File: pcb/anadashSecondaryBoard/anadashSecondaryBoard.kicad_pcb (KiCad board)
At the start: 2 copper layers, 198 x 35 mm, 12 parts, among them J2 LeftKeyConnector, J3 RightKeyConnector, J4 EncoderConnector, SW1 SW_Push, SW2 SW_Push, SW3 SW_Push, SW4 SW_Push, SW5 SW_Push, SW6 SW_Push, SW7 SW_Push, SW8 SW_Push, SW9 RotaryEncoder_Switch_MP

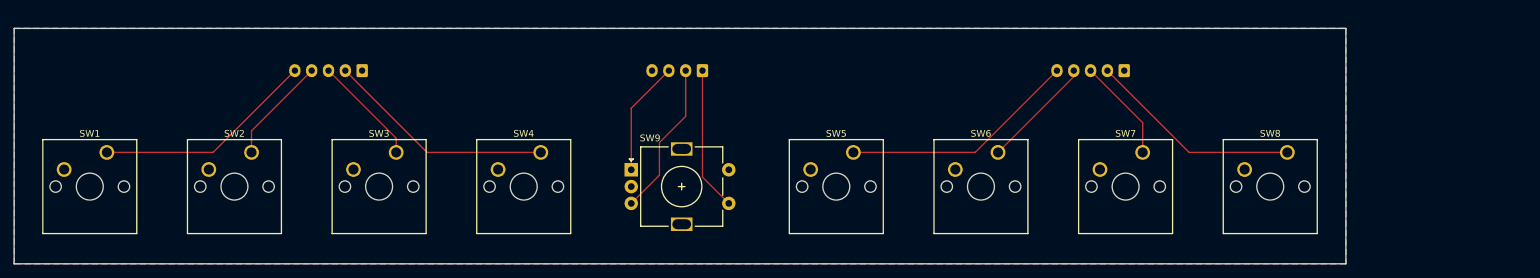
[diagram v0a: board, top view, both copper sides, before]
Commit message: Fixing alignment, improvements to pcb such as silkscreen.
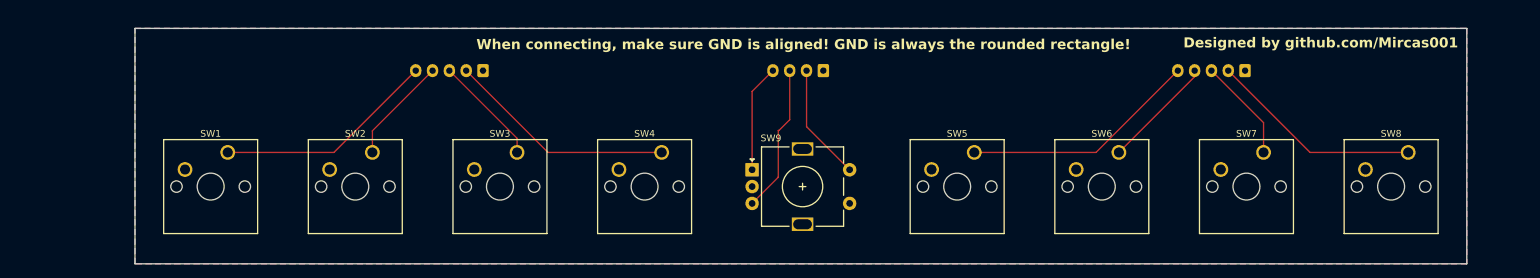
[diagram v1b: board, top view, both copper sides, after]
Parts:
- moved SW2 18.0 mm to (92.7, 90.6)
- moved SW4 18.0 mm to (135.7, 90.6)
- moved J2 18.0 mm to (109.2, 78.4)
- moved J3 18.0 mm to (222.5, 78.4)
- moved J4 18.0 mm to (159.8, 78.4)
- moved SW1 18.0 mm to (71.2, 90.6)
- moved SW3 18.0 mm to (114.2, 90.6)
- moved SW5 18.0 mm to (182.2, 90.6)
- moved SW6 18.0 mm to (203.7, 90.6)
- moved SW7 18.0 mm to (225.2, 90.6)
- moved SW8 18.0 mm to (246.7, 90.6)
- moved SW9 18.0 mm to (149.2, 93.1)
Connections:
- J4 pad 1: Net-(J4-Pin_1) -> GND
- J4 pad 4: GND -> Net-(J4-Pin_4)
- SW9 pad A: Net-(J4-Pin_3) -> Net-(J4-Pin_4)
- SW9 pad B: Net-(J4-Pin_2) -> Net-(J4-Pin_3)
- SW9 pad S1: Net-(J4-Pin_1) -> GND
- SW9 pad S2: GND -> Net-(J4-Pin_2)
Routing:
- net Net-(J4-Pin_1): track 21.4 -> 0.00 mm
- net Net-(J4-Pin_4): track 0.00 -> 16.0 mm
- net Net-(J4-Pin_2): track 23.1 -> 17.4 mm
- net Net-(J4-Pin_3): track 17.1 -> 22.1 mm
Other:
- board text added: "Designed by github.com/Mircas001"
- board text added: "When connecting, make sure GND is aligned! GND is always the rounded rectangle!"
- board text added: "When connecting, make sure GND is aligned! GND is always the rounded rectangle!r"

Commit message: both pcbs are done, but readme is bad
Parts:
- SW1, SW2, SW3, SW4, SW5, SW6, SW7, SW8: footprint Library:SW_Cherry_MX_1.00u_PCB -> footprints:SW_Cherry_MX_1.00u_PCB
- SW9: footprint Library:RotaryEncoder_Alps_EC11E-Switch_Vertical_H20mm -> footprints:RotaryEncoder_Alps_EC11E-Switch_Vertical_H20mm
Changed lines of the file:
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@@
 		)
 	)
-	(footprint "Library:SW_Cherry_MX_1.00u_PCB"
+	(footprint "footprints:SW_Cherry_MX_1.00u_PCB"
 		(layer "F.Cu")
 		(at 135.733572 90.56)
@@
 		)
 	)
-	(footprint "Library:RotaryEncoder_Alps_EC11E-Switch_Vertical_H20mm"
+	(footprint "footprints:RotaryEncoder_Alps_EC11E-Switch_Vertical_H20mm"
 		(layer "F.Cu")
 		(at 149.178572 93.14)
@@
 		(model "../3dmodels/EC11.STEP"
 			(offset
-				(xyz 7.25 -2.5 0)
+				(xyz 7.5 -2.5 0)
 			)
 			(scale
@@
 		)
 	)
-	(footprint "Library:SW_Cherry_MX_1.00u_PCB"
+	(footprint "footprints:SW_Cherry_MX_1.00u_PCB"
 		(layer "F.Cu")
 		(at 92.723572 90.56)
@@
 		)
 	)
-	(footprint "Library:SW_Cherry_MX_1.00u_PCB"
+	(footprint "footprints:SW_Cherry_MX_1.00u_PCB"
 		(layer "F.Cu")
 		(at 203.708572 90.56)
@@
 		)
 	)
-	(footprint "Library:SW_Cherry_MX_1.00u_PCB"
+	(footprint "footprints:SW_Cherry_MX_1.00u_PCB"
 		(layer "F.Cu")
 		(at 182.203572 90.56)
@@
 		)
 	)
-	(footprint "Library:SW_Cherry_MX_1.00u_PCB"
+	(footprint "footprints:SW_Cherry_MX_1.00u_PCB"
 		(layer "F.Cu")
 		(at 225.213572 90.56)
@@
 		)
 	)
-	(footprint "Library:SW_Cherry_MX_1.00u_PCB"
+	(footprint "footprints:SW_Cherry_MX_1.00u_PCB"
 		(layer "F.Cu")
 		(at 114.228572 90.56)
@@
 		)
 	)
-	(footprint "Library:SW_Cherry_MX_1.00u_PCB"
+	(footprint "footprints:SW_Cherry_MX_1.00u_PCB"
 		(layer "F.Cu")
 		(at 71.218572 90.56)
@@
 		)
 	)
-	(footprint "Library:SW_Cherry_MX_1.00u_PCB"
+	(footprint "footprints:SW_Cherry_MX_1.00u_PCB"
 		(layer "F.Cu")
 		(at 246.718572 90.56)

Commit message: change to thermal relief pads
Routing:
- net Net-(J4-Pin_3): track 22.1 -> 23.2 mm
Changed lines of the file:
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@@
 	)
 	(footprint "footprints:RotaryEncoder_Alps_EC11E-Switch_Vertical_H20mm"
+		(locked yes)
 		(layer "F.Cu")
 		(at 149.178572 93.14)
@@
 			(pinfunction "C_C")
 			(pintype "passive")
+			(thermal_bridge_angle 0)
 		)
 		(pad "MP" thru_hole rect
@@
 	)
 	(segment
-		(start 153.068572 94.25)
-		(end 149.178572 98.14)
+		(start 150.218572 97.1)
+		(end 152.1 97.1)
 		(width 0.2)
-		(layer "F.Cu")
+		(layer "B.Cu")
 		(net "Net-(J4-Pin_3)")
 	)
 	(segment
-		(start 154.768572 78.4)
-		(end 154.768572 85.7)
+		(start 153.1 96.1)
+		(end 153.1 87.7)
 		(width 0.2)
-		(layer "F.Cu")
+		(layer "B.Cu")
 		(net "Net-(J4-Pin_3)")
 	)
 	(segment
-		(start 154.768572 85.7)
-		(end 153.168572 87.3)
+		(start 153.1 87.7)
+		(end 154.768572 86.031428)
 		(width 0.2)
-		(layer "F.Cu")
+		(layer "B.Cu")
 		(net "Net-(J4-Pin_3)")
 	)
 	(segment
-		(start 153.068572 87.3)
-		(end 153.068572 94.25)
+		(start 154.768572 86.031428)
+		(end 154.768572 78.4)
 		(width 0.2)
-		(layer "F.Cu")
+		(layer "B.Cu")
 		(net "Net-(J4-Pin_3)")
 	)
 	(segment
-		(start 153.168572 87.3)
-		(end 153.068572 87.3)
+		(start 152.1 97.1)
+		(end 153.1 96.1)
 		(width 0.2)
-		(layer "F.Cu")
+		(layer "B.Cu")
+		(net "Net-(J4-Pin_3)")
+	)
+	(segment
+		(start 149.178572 98.14)
+		(end 150.218572 97.1)
+		(width 0.2)
+		(layer "B.Cu")
 		(net "Net-(J4-Pin_3)")
 	)
@@
 		(layers "F.Cu" "B.Cu")
 		(hatch edge 0.5)
-		(connect_pads yes
+		(connect_pads thru_hole_only
 			(clearance 0.5)
 		)
@@
 		)
 	)
-	(group ""
-		(members "0f12f814-220b-4fa7-bded-07e6e53be911" "16d72e7f-2332-48fe-9537-ea62faaf0efb"
-			"1c8ed136-85dc-439a-8579-073cd71f1154" "1fa840e8-9c74-4bc4-9152-fcb2cd233544"
-			"242a41c4-eef6-46ef-b2dc-b1d552c45234" "281b8d39-f4c1-4964-bbd5-4d3fb87b324d"
-			"2de5b0a6-cd0f-4b76-96dd-e0fdb3ede1ed" "306e651c-ac4a-4698-9a9a-f56862870678"
-			"30ab3fb7-b894-4934-804c-56a624411aeb" "32ac82a4-0260-4cdf-bf04-31f05ff12d7d"
-			"33c49a1f-6165-45a7-8cfa-0ead94ac7a19" "39b09e6b-5a9f-46d6-9884-2452578d9518"
-			"3bbb6232-8fb3-41cd-aa61-988be3443e9f" "3ea019b9-4416-4cec-95a5-aa135808d2b0"
-			"3f76182d-60ac-4dad-bcb7-cb203dbfb77a" "4131cef5-4ebf-41fe-8300-4e1b26b1f060"
-			"4465f784-3e10-444c-a3af-c4948929c6f3" "4a68688f-2d7d-4942-b52d-e872fb8eeac9"
-			"50e80096-2b7e-425e-a61d-9414ecfcdc7f" "7101ce4e-c384-4663-bcec-ca7b873b4472"
-			"71d00a78-12df-4162-9284-11512ec1a421" "76892e68-83dc-4447-a6d1-31658ae6cd1e"
-			"83c737a8-43e3-4f41-b59b-709531aff39a" "99416bc7-77ac-4d4f-8369-b6dc2d0a14d0"
-			"99d19ec8-dcc7-4a67-aef2-219197568392" "9a2c10ef-22ce-43b0-969c-0325b5092a9f"
-			"9a71fbdc-f945-41be-9da8-3076dc4176ea" "9df4c17d-7be7-4ac3-957f-47c9a74937f9"
-			"a13f49d3-85d9-4ebb-beb6-5224363cae6d" "ad9881e5-1c06-47a8-bbcb-b57efef70b94"
-			"be8d51fd-965b-409d-9617-b817fc5378af" "d0950714-24c7-4e71-99c8-6cd782e1f66e"
-			"d753b965-6750-417f-87c8-a1c8d05a13c2" "d7aea59e-14c1-4e6e-b328-f864be5f81d2"
-			"d8574bb3-1ac7-4304-8644-7f9b52ac90fe" "e7410d55-f5ab-49a3-811e-e4b2b80e9515"
-			"eb428ab5-ca8e-4d74-a038-ee8c859b7257" "ef372221-cd30-4211-a66d-6fcc45894a11"
-			"f0d50f6a-931b-45fa-8a8b-5cc49fbcc519"
-		)
-	)

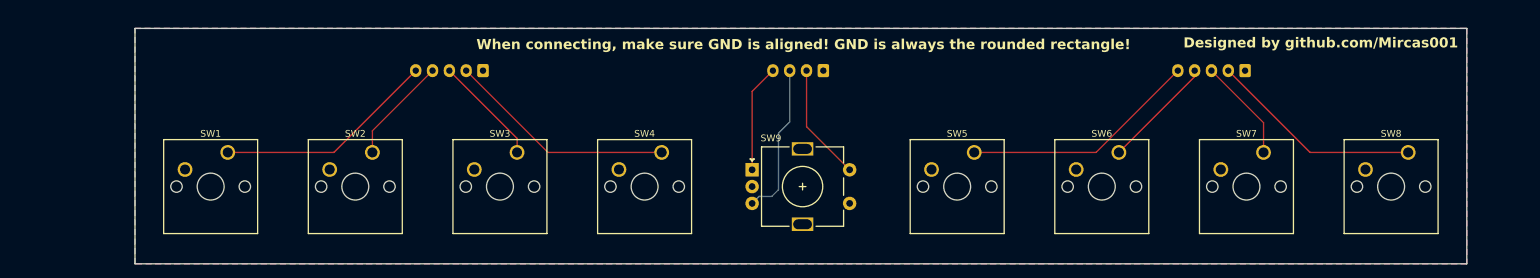
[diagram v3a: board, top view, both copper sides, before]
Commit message: removed assets, added mounting holes, made the aux pcb smaller
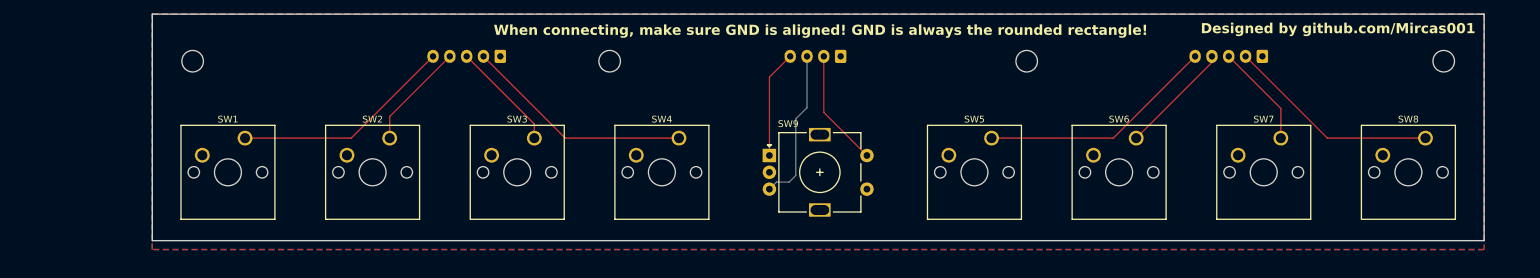
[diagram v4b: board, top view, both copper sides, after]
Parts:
- added REF**: MountingHole_3.2mm_M3, MountingHole:MountingHole_3.2mm_M3, F.Cu at (66.0, 77.0)
- added REF**: MountingHole_3.2mm_M3, MountingHole:MountingHole_3.2mm_M3, F.Cu at (128.0, 77.0)
- added REF**: MountingHole_3.2mm_M3, MountingHole:MountingHole_3.2mm_M3, F.Cu at (190.0, 77.0)
- added REF**: MountingHole_3.2mm_M3, MountingHole:MountingHole_3.2mm_M3, F.Cu at (252.0, 77.0)
- moved SW1 3.33 mm to (73.8, 88.4)
- moved J2 3.33 mm to (111.7, 76.3)
- moved J3 3.33 mm to (225.0, 76.3)
- moved J4 3.33 mm to (162.3, 76.3)
- moved SW2 3.33 mm to (95.3, 88.4)
- moved SW3 3.33 mm to (116.8, 88.4)
- moved SW4 3.33 mm to (138.3, 88.4)
- moved SW5 3.33 mm to (184.8, 88.4)
- moved SW6 3.33 mm to (206.3, 88.4)
- moved SW7 3.33 mm to (227.8, 88.4)
- moved SW8 3.33 mm to (249.3, 88.4)
- moved SW9 3.33 mm to (151.8, 91.0)
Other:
- board size 198 x 35 mm -> 198 x 33.7 mm

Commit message: Added folk valley cat and hamster to the PCB
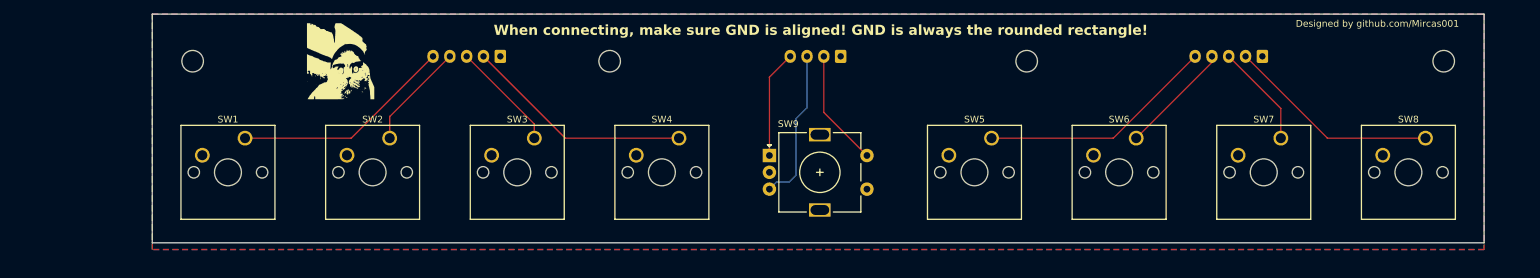
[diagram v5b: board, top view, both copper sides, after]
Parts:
- added G***: LOGO, Designs:tinycat, F.Cu at (88.0, 77.0)
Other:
- board size 198 x 33.7 mm -> 198 x 34 mm
